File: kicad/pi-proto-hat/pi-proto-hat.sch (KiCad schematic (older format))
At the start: 10 parts, among them J1 Conn_01x22_Male, J2 Conn_02x22_Top_Bottom, P1 Conn_02x20_Odd_Even

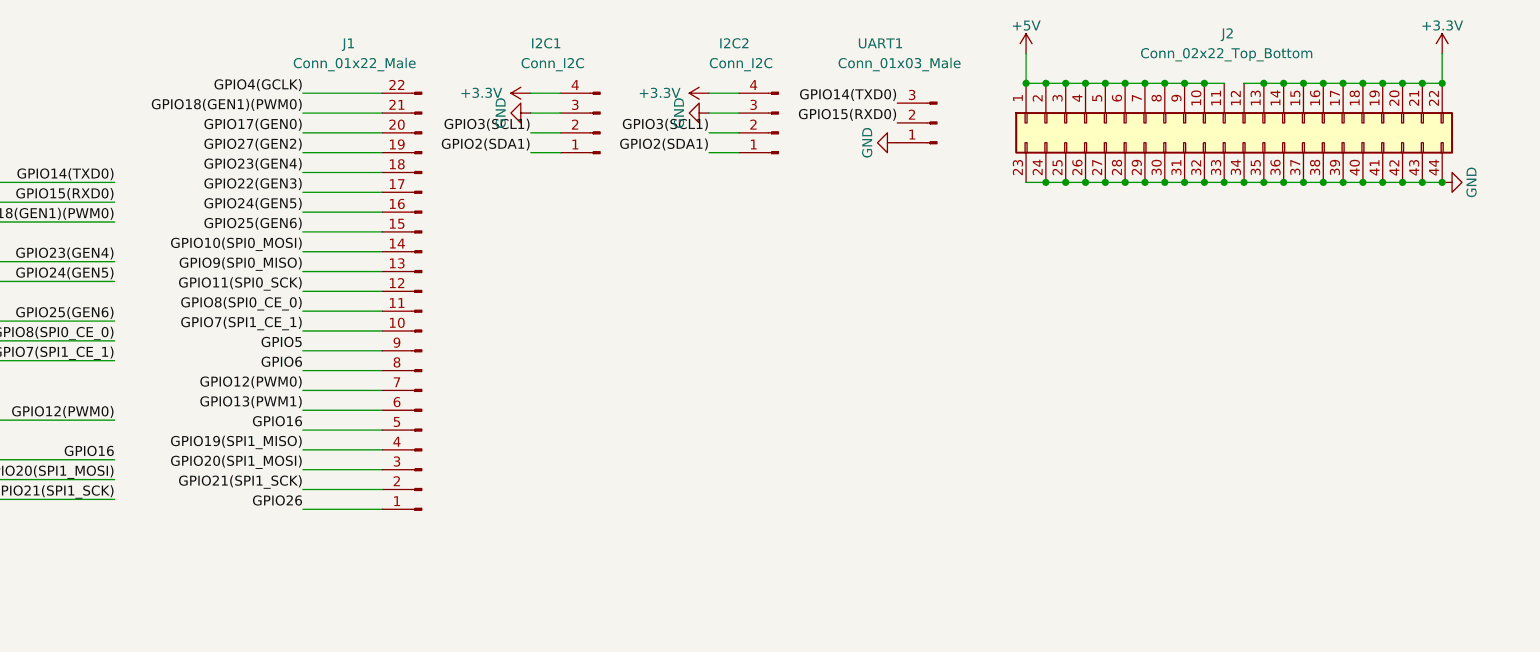
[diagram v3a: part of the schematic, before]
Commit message: changed footprints, added two prototype-areas
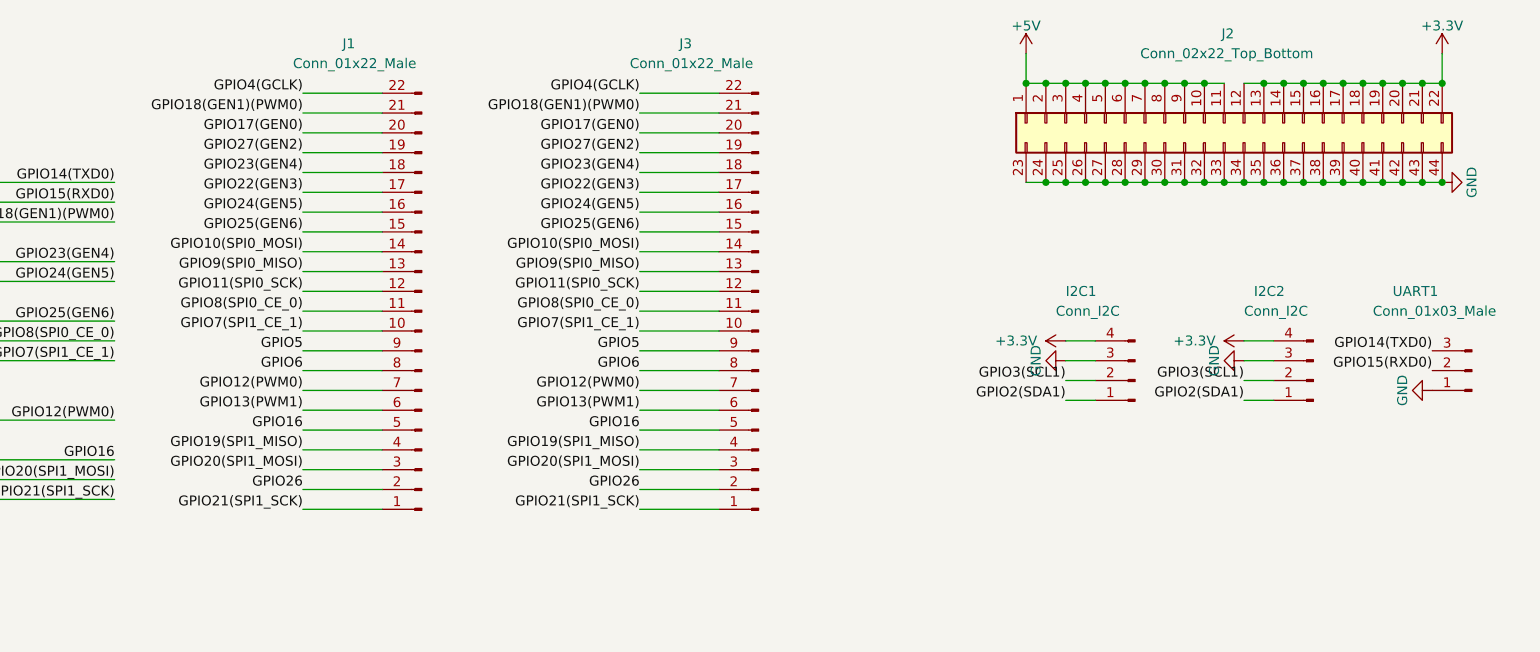
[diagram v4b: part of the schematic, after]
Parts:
- added J3: Conn_01x22_Male, Proto_Area:Proto_Area_22x01, symbol Connector:Conn_01x22_Male
- I2C1, I2C2: footprint Connector_PinHeader_2.54mm:PinHeader_1x04_P2.54mm_Vertical -> Proto_Area:Proto_Area_04x01
- J1: footprint Connector_PinHeader_2.54mm:PinHeader_1x22_P2.54mm_Vertical -> Proto_Area:Proto_Area_22x01
- UART1: footprint Connector_PinHeader_2.54mm:PinHeader_1x03_P2.54mm_Vertical -> Proto_Area:Proto_Area_03x01
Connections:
- net GPIO10(SPI0_MOSI): now also J3.14 (Pin_14)
- net GPIO11(SPI0_SCK): now also J3.12 (Pin_12)
- net GPIO12(PWM0): now also J3.7 (Pin_7)
- net GPIO13(PWM1): now also J3.6 (Pin_6)
- net GPIO16: now also J3.5 (Pin_5)
- net GPIO17(GEN0): now also J3.20 (Pin_20)
- net GPIO18(GEN1)(PWM0): now also J3.21 (Pin_21)
- net GPIO19(SPI1_MISO): now also J3.4 (Pin_4)
- net GPIO20(SPI1_MOSI): now also J3.3 (Pin_3)
- net GPIO21(SPI1_SCK): now also J1.1 (Pin_1), J3.1 (Pin_1); no longer J1.2 (Pin_2)
- net GPIO22(GEN3): now also J3.17 (Pin_17)
- net GPIO23(GEN4): now also J3.18 (Pin_18)
- net GPIO24(GEN5): now also J3.16 (Pin_16)
- net GPIO25(GEN6): now also J3.15 (Pin_15)
- net GPIO26: now also J1.2 (Pin_2), J3.2 (Pin_2); no longer J1.1 (Pin_1)
- net GPIO27(GEN2): now also J3.19 (Pin_19)
- net GPIO4(GCLK): now also J3.22 (Pin_22)
- net GPIO5: now also J3.9 (Pin_9)
- net GPIO6: now also J3.8 (Pin_8)
- net GPIO7(SPI1_CE_1): now also J3.10 (Pin_10)
- net GPIO8(SPI0_CE_0): now also J3.11 (Pin_11)
- net GPIO9(SPI0_MISO): now also J3.13 (Pin_13)
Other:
- moved on the sheet: I2C1, I2C2, UART1
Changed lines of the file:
@@
 F 0 "J1" H 5900 700 50  0000 R CNN
 F 1 "Conn_01x22_Male" H 6150 800 50  0000 R CNN
-F 2 "Connector_PinHeader_2.54mm:PinHeader_1x22_P2.54mm_Vertical" H 5500 2050 50  0001 C CNN
+F 2 "Proto_Area:Proto_Area_22x01" H 5500 2050 50  0001 C CNN
 F 3 "~" H 5500 2050 50  0001 C CNN
 	1    5500 2050
@@
 Text Label 4900 2850 2    50   ~ 0
 GPIO20(SPI1_MOSI)
+Text Label 4900 3050 2    50   ~ 0
+GPIO21(SPI1_SCK)
 Text Label 4900 2950 2    50   ~ 0
-GPIO21(SPI1_SCK)
-Text Label 4900 3050 2    50   ~ 0
 GPIO26
 Wire Wire Line
@@
 L Connector:Conn_01x04_Male I2C1
 U 1 1 5E3AE486
-P 6400 1150
-F 0 "I2C1" H 6750 700 50  0000 R CNN
-F 1 "Conn_I2C" H 6800 800 50  0000 R CNN
-F 2 "Connector_PinHeader_2.54mm:PinHeader_1x04_P2.54mm_Vertical" H 6400 1150 50  0001 C CNN
-F 3 "~" H 6400 1150 50  0001 C CNN
-	1    6400 1150
+P 9100 2400
+F 0 "I2C1" H 9450 1950 50  0000 R CNN
+F 1 "Conn_I2C" H 9500 2050 50  0000 R CNN
+F 2 "Proto_Area:Proto_Area_04x01" H 9100 2400 50  0001 C CNN
+F 3 "~" H 9100 2400 50  0001 C CNN
+	1    9100 2400
 	-1   0    0    1
 $EndComp
@@
 L power:+3.3V #PWR0104
 U 1 1 5E3B69CB
-P 6050 950
-F 0 "#PWR0104" H 6050 800 50  0001 C CNN
-F 1 "+3.3V" V 6050 1200 50  0000 C CNN
-F 2 "" H 6050 950 50  0000 C CNN
-F 3 "" H 6050 950 50  0000 C CNN
-	1    6050 950
+P 8750 2200
+F 0 "#PWR0104" H 8750 2050 50  0001 C CNN
+F 1 "+3.3V" V 8750 2450 50  0000 C CNN
+F 2 "" H 8750 2200 50  0000 C CNN
+F 3 "" H 8750 2200 50  0000 C CNN
+	1    8750 2200
 	0    -1   -1   0
 $EndComp
@@
 L power:GND #PWR0105
 U 1 1 5E3BF524
-P 6050 1050
-F 0 "#PWR0105" H 6050 800 50  0001 C CNN
-F 1 "GND" H 6050 900 50  0000 C CNN
-F 2 "" H 6050 1050 50  0000 C CNN
-F 3 "" H 6050 1050 50  0000 C CNN
-	1    6050 1050
+P 8750 2300
+F 0 "#PWR0105" H 8750 2050 50  0001 C CNN
+F 1 "GND" H 8750 2150 50  0000 C CNN
+F 2 "" H 8750 2300 50  0000 C CNN
+F 3 "" H 8750 2300 50  0000 C CNN
+	1    8750 2300
 	0    1    1    0
 $EndComp
-Text Label 6050 1150 2    50   ~ 0
+Text Label 8750 2400 2    50   ~ 0
 GPIO3(SCL1)
-Text Label 6050 1250 2    50   ~ 0
+Text Label 8750 2500 2    50   ~ 0
 GPIO2(SDA1)
 Wire Wire Line
-	6050 950  6200 950
-Wire Wire Line
-	6050 1050 6200 1050
-Wire Wire Line
-	6050 1150 6200 1150
-Wire Wire Line
-	6050 1250 6200 1250
+	8750 2200 8900 2200
+Wire Wire Line
+	8750 2300 8900 2300
+Wire Wire Line
+	8750 2400 8900 2400
+Wire Wire Line
+	8750 2500 8900 2500
 $Comp
 L Connector:Conn_01x04_Male I2C2
 U 1 1 5E46D17D
-P 7300 1150
-F 0 "I2C2" H 7600 700 50  0000 R CNN
-F 1 "Conn_I2C" H 7650 800 50  0000 R CNN
-F 2 "Connector_PinHeader_2.54mm:PinHeader_1x04_P2.54mm_Vertical" H 7300 1150 50  0001 C CNN
-F 3 "~" H 7300 1150 50  0001 C CNN
-	1    7300 1150
+P 10000 2400
+F 0 "I2C2" H 10300 1950 50  0000 R CNN
+F 1 "Conn_I2C" H 10350 2050 50  0000 R CNN
+F 2 "Proto_Area:Proto_Area_04x01" H 10000 2400 50  0001 C CNN
+F 3 "~" H 10000 2400 50  0001 C CNN
+	1    10000 2400
 	-1   0    0    1
 $EndComp
@@
 L power:+3.3V #PWR0106
 U 1 1 5E46D187
-P 6950 950
-F 0 "#PWR0106" H 6950 800 50  0001 C CNN
-F 1 "+3.3V" V 6950 1200 50  0000 C CNN
-F 2 "" H 6950 950 50  0000 C CNN
-F 3 "" H 6950 950 50  0000 C CNN
-	1    6950 950
+P 9650 2200
+F 0 "#PWR0106" H 9650 2050 50  0001 C CNN
+F 1 "+3.3V" V 9650 2450 50  0000 C CNN
+F 2 "" H 9650 2200 50  0000 C CNN
+F 3 "" H 9650 2200 50  0000 C CNN
+	1    9650 2200
 	0    -1   -1   0
 $EndComp
@@
 L power:GND #PWR0107
 U 1 1 5E46D191
-P 6950 1050
-F 0 "#PWR0107" H 6950 800 50  0001 C CNN
-F 1 "GND" H 6950 900 50  0000 C CNN
-F 2 "" H 6950 1050 50  0000 C CNN
-F 3 "" H 6950 1050 50  0000 C CNN
-	1    6950 1050
+P 9650 2300
+F 0 "#PWR0107" H 9650 2050 50  0001 C CNN
+F 1 "GND" H 9650 2150 50  0000 C CNN
+F 2 "" H 9650 2300 50  0000 C CNN
+F 3 "" H 9650 2300 50  0000 C CNN
+	1    9650 2300
 	0    1    1    0
 $EndComp
-Text Label 6950 1150 2    50   ~ 0
+Text Label 9650 2400 2    50   ~ 0
 GPIO3(SCL1)
-Text Label 6950 1250 2    50   ~ 0
+Text Label 9650 2500 2    50   ~ 0
 GPIO2(SDA1)
 Wire Wire Line
-	6950 950  7100 950
-Wire Wire Line
-	6950 1050 7100 1050
-Wire Wire Line
-	6950 1150 7100 1150
-Wire Wire Line
-	6950 1250 7100 1250
+	9650 2200 9800 2200
+Wire Wire Line
+	9650 2300 9800 2300
+Wire Wire Line
+	9650 2400 9800 2400
+Wire Wire Line
+	9650 2500 9800 2500
 $Comp
 L Connector:Conn_01x03_Male UART1
 U 1 1 5E470F02
-P 8100 1100
-F 0 "UART1" H 8500 700 50  0000 R CNN
-F 1 "Conn_01x03_Male" H 8600 800 50  0000 R CNN
-F 2 "Connector_PinHeader_2.54mm:PinHeader_1x03_P2.54mm_Vertical" H 8100 1100 50  0001 C CNN
-F 3 "~" H 8100 1100 50  0001 C CNN
-	1    8100 1100
+P 10800 2350
+F 0 "UART1" H 11200 1950 50  0000 R CNN
+F 1 "Conn_01x03_Male" H 11300 2050 50  0000 R CNN
+F 2 "Proto_Area:Proto_Area_03x01" H 10800 2350 50  0001 C CNN
+F 3 "~" H 10800 2350 50  0001 C CNN
+	1    10800 2350
 	-1   0    0    1
 $EndComp
-Text Label 7900 1000 2    50   ~ 0
+Text Label 10600 2250 2    50   ~ 0
 GPIO14(TXD0)
-Text Label 7900 1100 2    50   ~ 0
+Text Label 10600 2350 2    50   ~ 0
 GPIO15(RXD0)
 $Comp
 L power:GND #PWR0108
 U 1 1 5E4850A5
-P 7900 1200
-F 0 "#PWR0108" H 7900 950 50  0001 C CNN
-F 1 "GND" H 7900 1050 50  0000 C CNN
-F 2 "" H 7900 1200 50  0000 C CNN
-F 3 "" H 7900 1200 50  0000 C CNN
-	1    7900 1200
+P 10600 2450
+F 0 "#PWR0108" H 10600 2200 50  0001 C CNN
+F 1 "GND" H 10600 2300 50  0000 C CNN
+F 2 "" H 10600 2450 50  0000 C CNN
+F 3 "" H 10600 2450 50  0000 C CNN
+	1    10600 2450
 	0    1    1    0
 $EndComp
@@
 Wire Wire Line
 	4900 2950 5300 2950
+$Comp
+L Connector:Conn_01x22_Male J3
+U 1 1 5E49AAAC
+P 7200 2050
+F 0 "J3" H 7600 700 50  0000 R CNN
+F 1 "Conn_01x22_Male" H 7850 800 50  0000 R CNN
+F 2 "Proto_Area:Proto_Area_22x01" H 7200 2050 50  0001 C CNN
+F 3 "~" H 7200 2050 50  0001 C CNN
+	1    7200 2050
+	-1   0    0    1
+$EndComp
+Text Label 6600 950  2    50   ~ 0
+GPIO4(GCLK)
+Text Label 6600 1150 2    50   ~ 0
+GPIO17(GEN0)
+Text Label 6600 1050 2    50   ~ 0
+GPIO18(GEN1)(PWM0)
+Text Label 6600 1250 2    50   ~ 0
+GPIO27(GEN2)
+Text Label 6600 1450 2    50   ~ 0
+GPIO22(GEN3)
+Text Label 6600 1650 2    50   ~ 0
+GPIO25(GEN6)
+Text Label 6600 1750 2    50   ~ 0
+GPIO10(SPI0_MOSI)
+Text Label 6600 1850 2    50   ~ 0
+GPIO9(SPI0_MISO)
+Text Label 6600 1950 2    50   ~ 0
+GPIO11(SPI0_SCK)
+Text Label 6600 2050 2    50   ~ 0
+GPIO8(SPI0_CE_0)
+Text Label 6600 2150 2    50   ~ 0
+GPIO7(SPI1_CE_1)
+Text Label 6600 2250 2    50   ~ 0
+GPIO5
+Text Label 6600 2350 2    50   ~ 0
+GPIO6
+Text Label 6600 2450 2    50   ~ 0
+GPIO12(PWM0)
+Text Label 6600 2550 2    50   ~ 0
+GPIO13(PWM1)
+Text Label 6600 2650 2    50   ~ 0
+GPIO16
+Text Label 6600 2750 2    50   ~ 0
+GPIO19(SPI1_MISO)
+Text Label 6600 2850 2    50   ~ 0
+GPIO20(SPI1_MOSI)
+Text Label 6600 3050 2    50   ~ 0
+GPIO21(SPI1_SCK)
+Text Label 6600 2950 2    50   ~ 0
+GPIO26
+Wire Wire Line
+	6600 950  7000 950
+Wire Wire Line
+	6600 1050 7000 1050
+Wire Wire Line
+	6600 1150 7000 1150
+Wire Wire Line
+	6600 1250 7000 1250
+Wire Wire Line
+	6600 1350 7000 1350
+Wire Wire Line
+	6600 1450 7000 1450
+Wire Wire Line
+	6600 1550 7000 1550
+Wire Wire Line
+	6600 1650 7000 1650
+Wire Wire Line
+	6600 1750 7000 1750
+Wire Wire Line
+	6600 1850 7000 1850
+Wire Wire Line
+	6600 1950 7000 1950
+Wire Wire Line
+	6600 2050 7000 2050
+Wire Wire Line
+	6600 2150 7000 2150
+Wire Wire Line
+	6600 2250 7000 2250
+Wire Wire Line
+	6600 2550 7000 2550
+Wire Wire Line
+	6600 2650 7000 2650
+Wire Wire Line
+	6600 2750 7000 2750
+Wire Wire Line
+	6600 3050 7000 3050
+Text Label 6600 1550 2    50   ~ 0
+GPIO24(GEN5)
+Text Label 6600 1350 2    50   ~ 0
+GPIO23(GEN4)
+Wire Wire Line
+	6600 2350 7000 2350
+Wire Wire Line
+	6600 2850 7000 2850
+Wire Wire Line
+	6600 2450 7000 2450
+Wire Wire Line
+	6600 2950 7000 2950
 $EndSCHEMATC
